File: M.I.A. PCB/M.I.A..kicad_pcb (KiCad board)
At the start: 6 copper layers, 50.8 x 106.6 mm, 159 parts, among them J1 USB_C_Receptacle_USB2.0_16P, J10 Conn_01x03, J11 Conn_01x03, J12 Conn_Coaxial, J12 Screw_Terminal_01x02, J13 Screw_Terminal_01x02, J14 Screw_Terminal_01x02, J15 Screw_Terminal_01x02, J16 Screw_Terminal_01x02, J17 Screw_Terminal_01x02, J18 Screw_Terminal_01x02, J19 Conn_01x08_Socket, J2 Conn_01x02_Pin, J20 Screw_Terminal_01x02, J21 Conn_01x04_Socket, J22 Conn_01x04_Socket, J3 Conn_01x03, J4 Conn_01x03, J5 Conn_01x03, J6 Conn_01x03, J7 MSD-4-A, J8 Conn_01x03, J9 Conn_01x03, Q1 AO3400A, Q2 AO3400A, Q3 AO3400A, Q4 AO3400A, SW1 SW_Push, SW2 SW_Push, U1 W25Q128JVS, U10 AP2112K-3.3, U11 INA219AxDCN, U12 AP62150WU, U13 TPS2121RUXR, U14 AP62150WU, U15 74AHC541, U2 RP2350B-QFN80, U3 MMC5983MA, U4 ICM-45686, U5 MS5611-01BA, U6 TMP117xxDRV, U7 MAX-M10S, U8 KX134-1211, U9 TPS2121RUXR, Y1 ABM8-272-T3

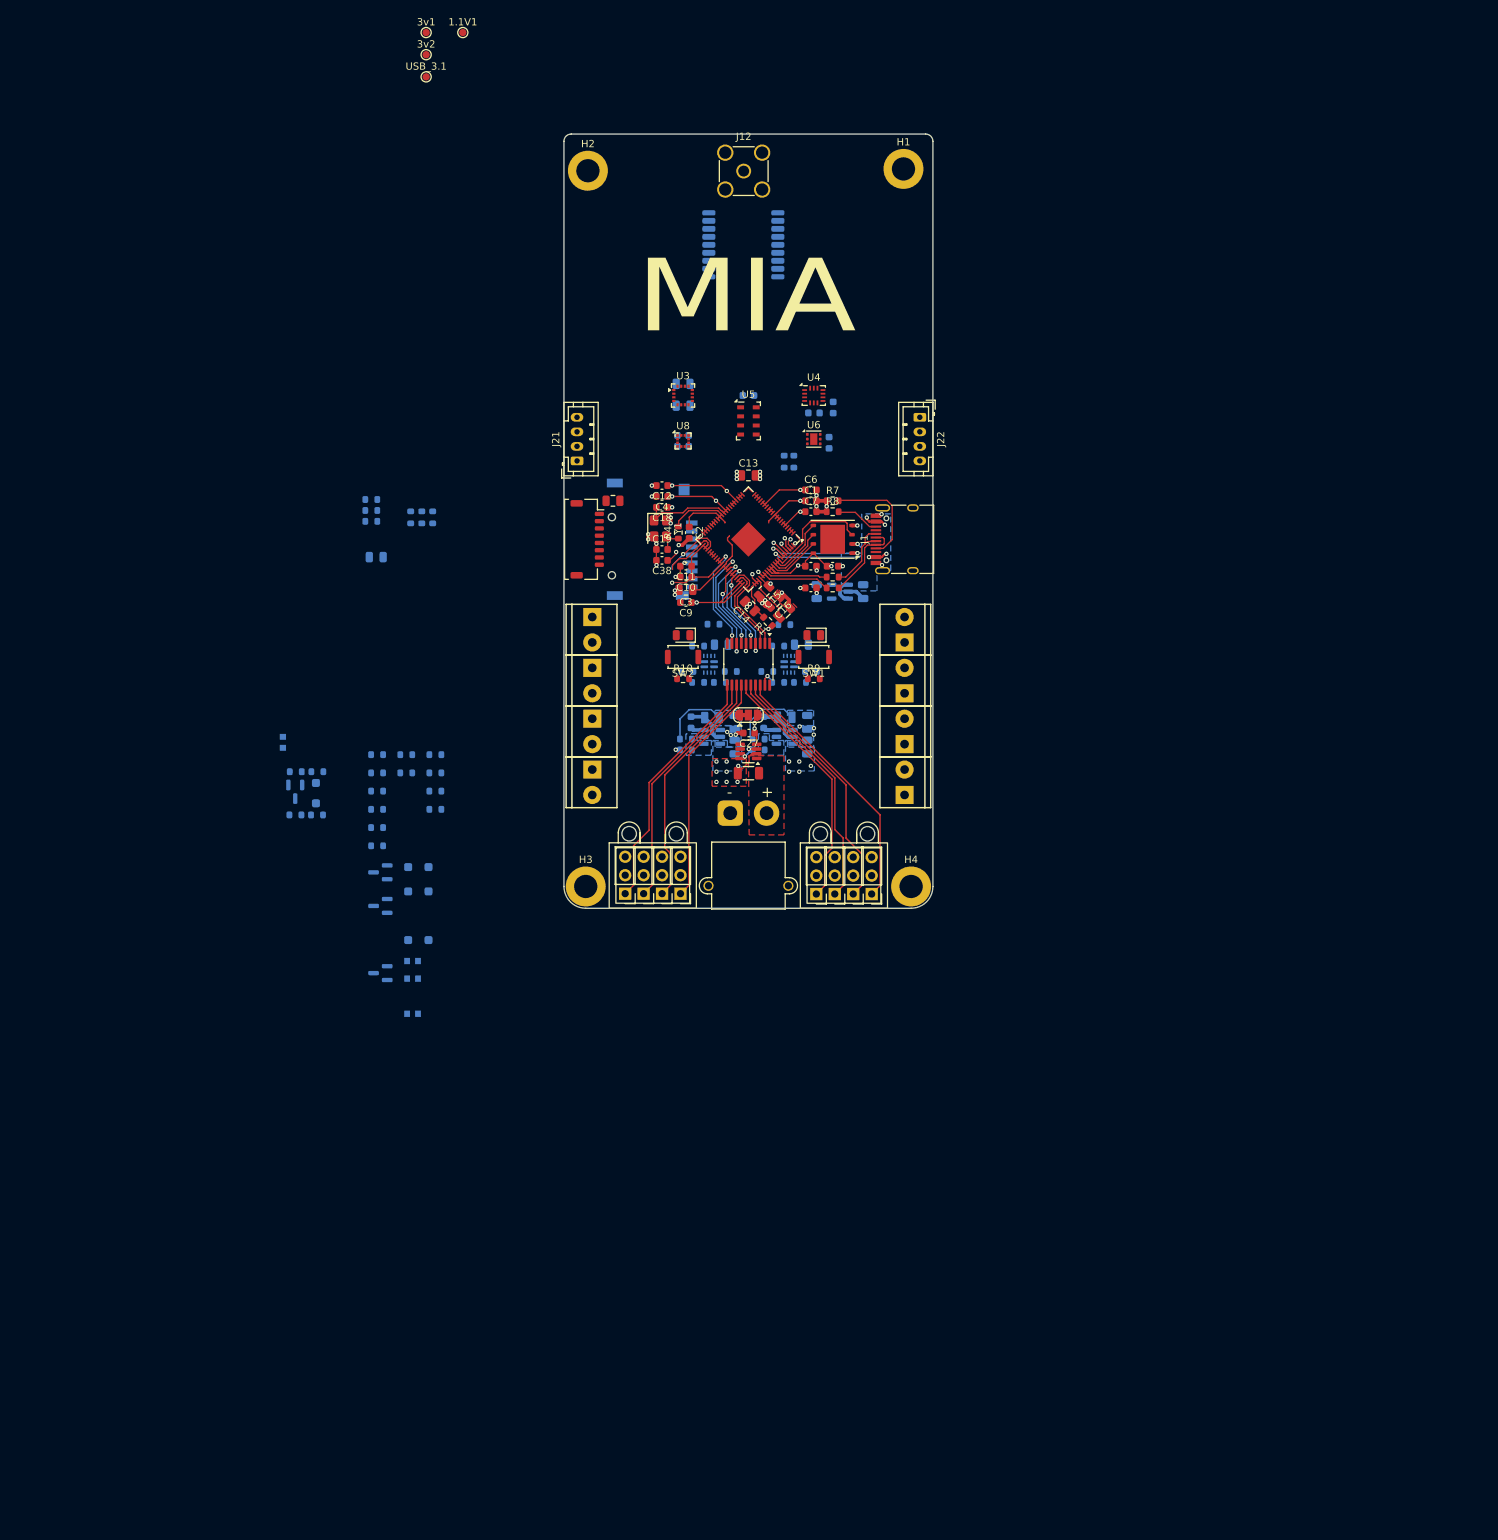
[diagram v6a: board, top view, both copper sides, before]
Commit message: Wired Sensors
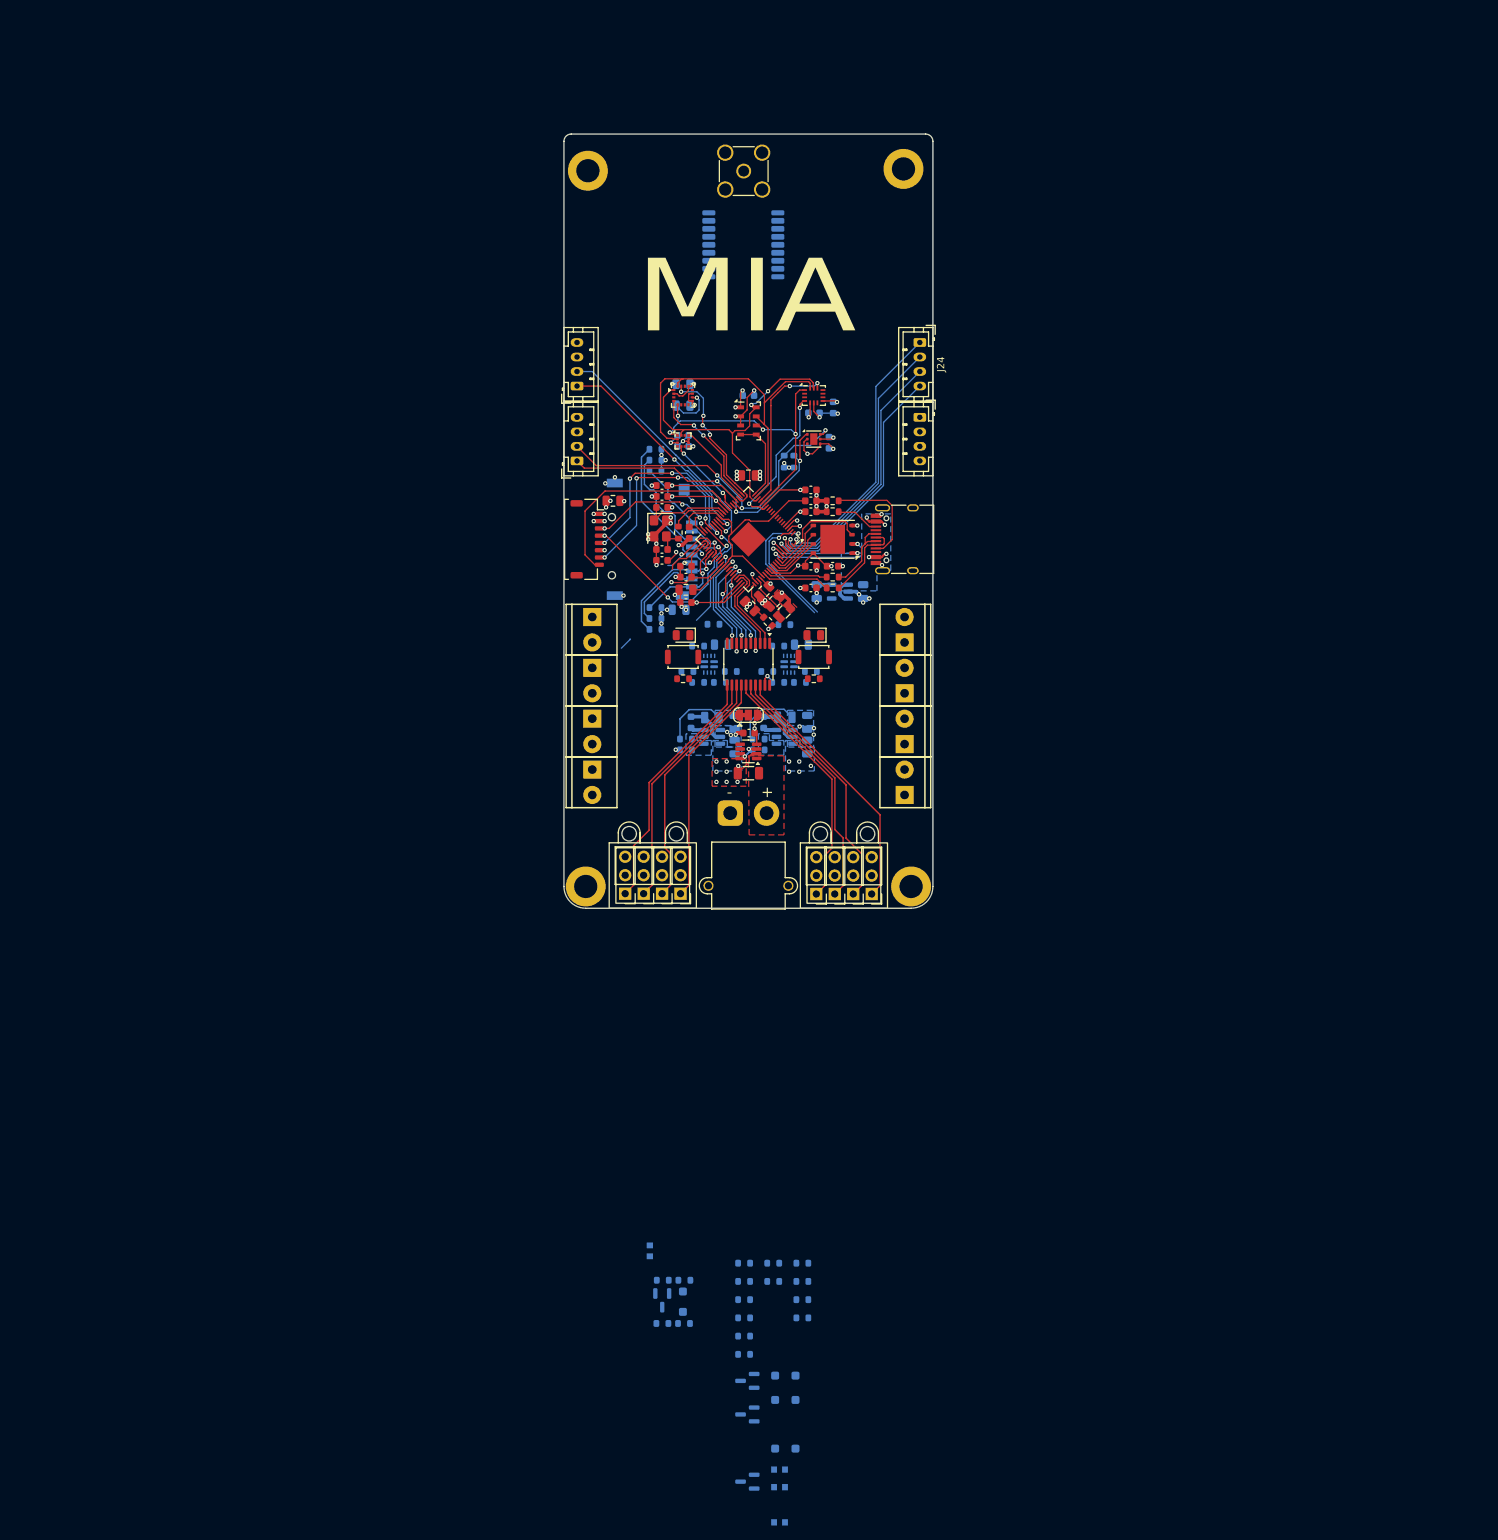
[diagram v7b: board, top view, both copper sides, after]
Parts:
- removed 1.1V1, 3v1, 3v2, USB_3.1: TestPoint, TestPoint:TestPoint_Pad_D1.0mm
- added J23: Conn_01x04_Socket, Connector_JST:JST_PH_B4B-PH-K_1x04_P2.00mm_Vertical, F.Cu at (21.8, 49.7)
- added J24: Conn_01x04_Socket, Connector_JST:JST_PH_B4B-PH-K_1x04_P2.00mm_Vertical, F.Cu at (69.0, 43.7)
- moved D4 86.3 mm to (50.5, 189.3)
- moved D5 86.3 mm to (36.4, 175.8)
- moved F3 86.3 mm to (31.8, 168.8)
- moved Q1 86.3 mm to (45.3, 186.7)
- moved Q2 86.3 mm to (45.3, 191.3)
- moved Q3 86.3 mm to (33.5, 175.6)
- moved Q4 86.3 mm to (45.3, 200.6)
- moved R34 86.3 mm to (44.8, 170.5)
- moved R35 86.3 mm to (44.8, 173.0)
- moved R36 86.3 mm to (44.8, 175.5)
- moved R37 86.3 mm to (44.8, 178.0)
- moved R38 86.3 mm to (44.8, 180.5)
- moved R39 86.3 mm to (44.8, 183.0)
- moved R40 86.3 mm to (48.8, 170.5)
- moved R41 86.3 mm to (48.8, 173.0)
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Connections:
- U2 pad 1: unconnected-(U2-GPIO4-Pad1) -> IGN_4
- U2 pad 14: unconnected-(U2-GPIO15-Pad14) -> IMU_INT1
- U2 pad 16: unconnected-(U2-GPIO16-Pad16) -> SPI_MISO_SEN
- U2 pad 17: unconnected-(U2-GPIO17-Pad17) -> IMU_CS
- U2 pad 18: unconnected-(U2-GPIO18-Pad18) -> SPI_SCK_SEN
- U2 pad 19: unconnected-(U2-GPIO19-Pad19) -> SPI_MOSI_SEN
- U2 pad 2: unconnected-(U2-GPIO5-Pad2) -> IGN_3
- U2 pad 20: unconnected-(U2-GPIO20-Pad20) -> BAR_CS
- U2 pad 21: unconnected-(U2-GPIO21-Pad21) -> MAG_CS
- U2 pad 22: unconnected-(U2-GPIO22-Pad22) -> ACC_CS
- U2 pad 23: unconnected-(U2-GPIO23-Pad23) -> MAG_INT
- U2 pad 25: unconnected-(U2-GPIO24-Pad25) -> SDA
- U2 pad 26: unconnected-(U2-GPIO25-Pad26) -> SCL
- U2 pad 27: unconnected-(U2-GPIO26-Pad27) -> ACC_INT
- U2 pad 28: unconnected-(U2-GPIO27-Pad28) -> RST_TLM
- U2 pad 33: unconnected-(U2-SWCLK-Pad33) -> SWCLK
- U2 pad 34: unconnected-(U2-SWDIO-Pad34) -> SWDIO
- U2 pad 36: unconnected-(U2-GPIO28-Pad36) -> SPI_MISO_TLM
- U2 pad 37: unconnected-(U2-GPIO29-Pad37) -> SPI_CS_TLM
- U2 pad 38: unconnected-(U2-GPIO30-Pad38) -> SPI_SCK_TLM
- U2 pad 39: IGN_4 -> SPI_MOSI_TLM
- U2 pad 40: IGN_3 -> D0_TLM
- U2 pad 77: unconnected-(U2-GPIO0-Pad77) -> GPIO1
- U2 pad 78: unconnected-(U2-GPIO1-Pad78) -> GPIO2
- U2 pad 79: unconnected-(U2-GPIO2-Pad79) -> GPIO3
- U2 pad 80: unconnected-(U2-GPIO3-Pad80) -> GPIO4
- U4 pad 9: IMU_INT2 -> unconnected-(U4-INT2/FSYNC/CLKIN-Pad9)
- U8 pad 4: ACC_TRIG -> GND
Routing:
- net SPI_MOSI_SEN: track 0.00 -> 51.1 mm
- net SDA: track 0.00 -> 47.2 mm, vias 0 -> 3
- net SPI_SCK_SEN: track 0.00 -> 45.1 mm, vias 0 -> 2
- net SCL: track 0.00 -> 44.6 mm, vias 0 -> 3
- net SPI_MISO_SEN: track 0.00 -> 42.3 mm, vias 0 -> 4
- net GND: track 55.0 -> 94.9 mm, vias 41 -> 62
- net GPIO4: track 0.00 -> 37.6 mm, vias 0 -> 1
- net GPIO2: track 0.00 -> 37.6 mm, vias 0 -> 1
- net GPIO3: track 0.00 -> 37.5 mm, vias 0 -> 1
- net GPIO1: track 0.00 -> 35.3 mm, vias 0 -> 1
- net SWDIO: track 0.00 -> 34.5 mm, vias 0 -> 1
- net +3.3V: track 81.2 -> 112.7 mm, vias 20 -> 39
- net SWCLK: track 0.00 -> 31.2 mm, vias 0 -> 2
- net RST_TLM: track 0.00 -> 30.6 mm
- net SPI_MISO_TLM: track 0.00 -> 30.6 mm, vias 0 -> 4
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- removed copper zone on In2.Cu, net +1V1

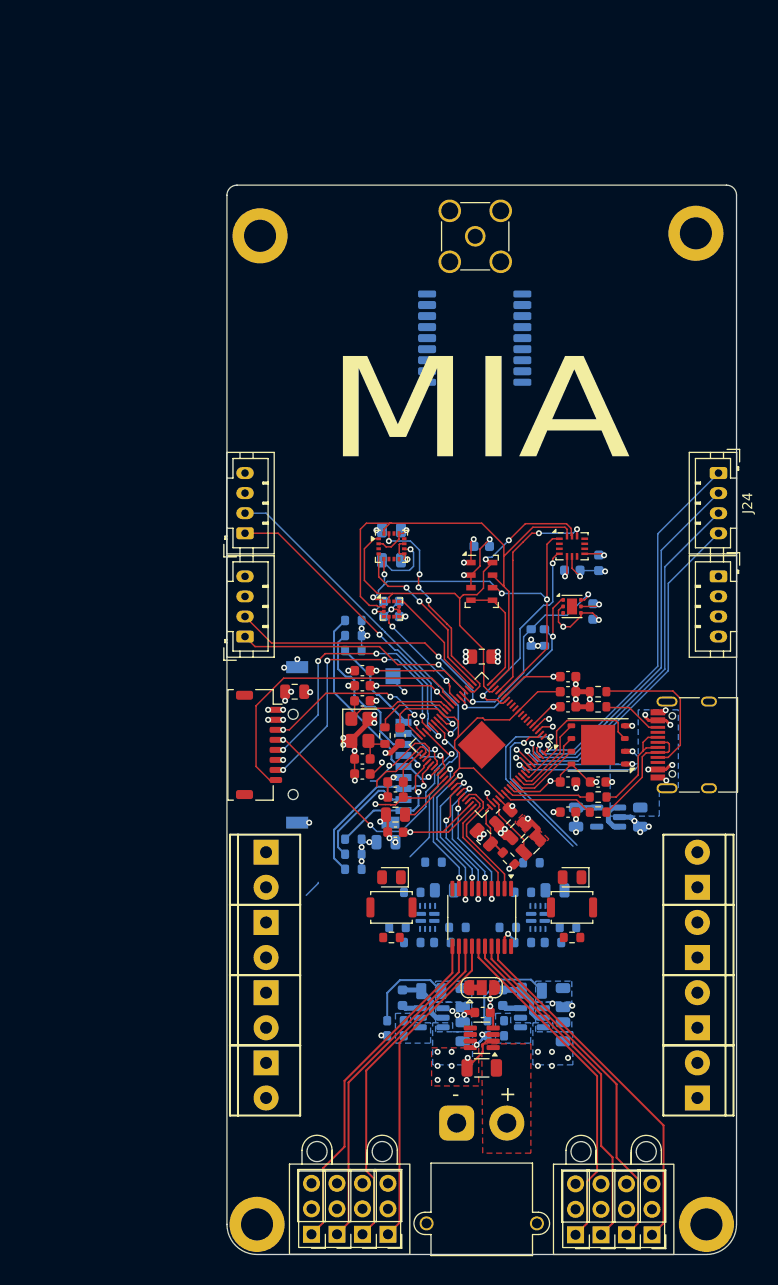
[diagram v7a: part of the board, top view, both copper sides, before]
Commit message: routed continuity sensing and pwm routing fixed
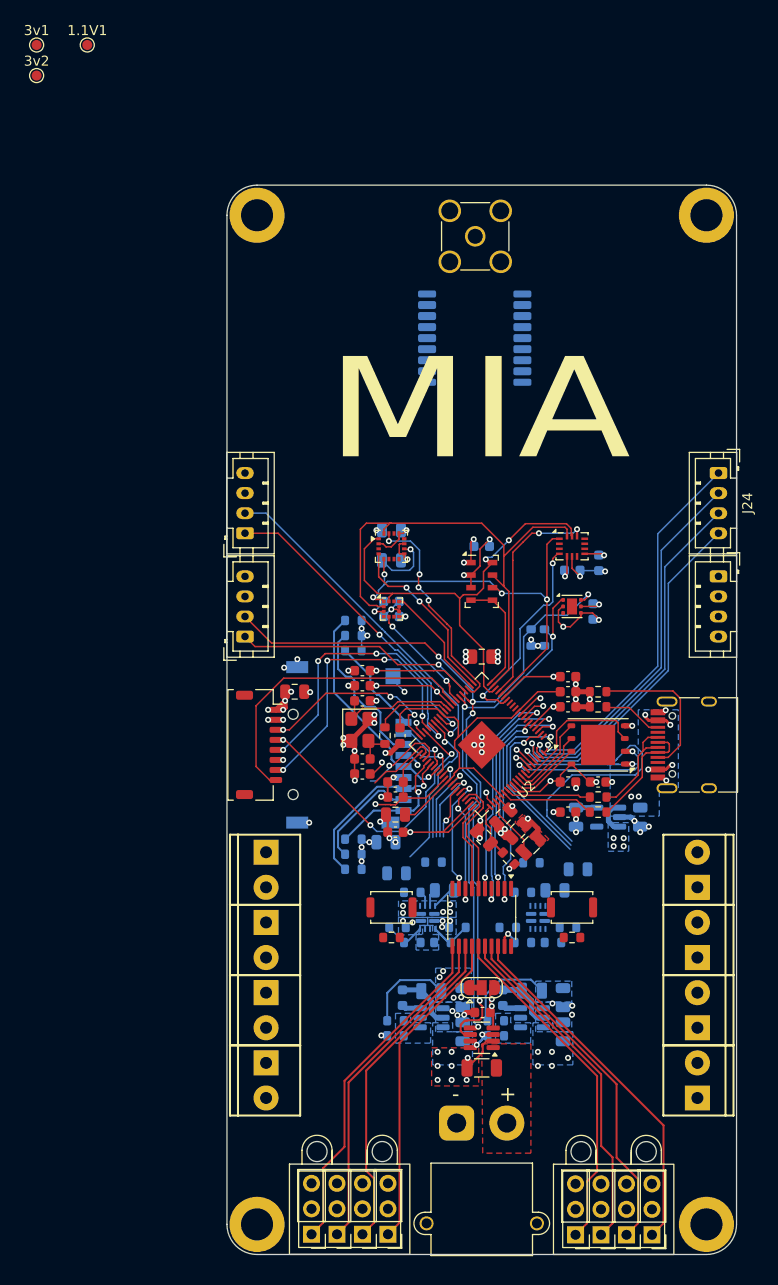
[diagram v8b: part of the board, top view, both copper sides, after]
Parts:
- added 1.1V1: TestPoint, TestPoint:TestPoint_Pad_D1.0mm, F.Cu at (6.08, 1.02)
- added 3v1: TestPoint, TestPoint:TestPoint_Pad_D1.0mm, F.Cu at (1.02, 1.02)
- added 3v2: TestPoint, TestPoint:TestPoint_Pad_D1.0mm, F.Cu at (1.02, 4.08)
- D1, D2: moved to B.Cu
- moved H1 2.08 mm to (67.8, 18.0)
- moved H2 2.07 mm to (23.0, 18.0)
- moved D1 1.00 mm to (55.0, 83.2), turned to 0 degrees
- moved D2 0.64 mm to (36.9, 83.6), turned to 0 degrees
- turned C34 to 0 degrees
- turned R25 to 180 degrees
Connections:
- U2 pad 3: unconnected-(U2-GPIO6-Pad3) -> PWM2
- U2 pad 4: unconnected-(U2-GPIO7-Pad4) -> PWM3
- U2 pad 49: PWM8 -> Cont_Sense4
- U2 pad 52: PWM7 -> Cont_Sense3
- U2 pad 53: PWM6 -> Cont_Sense2
- U2 pad 54: PWM5 -> Cont_Sense1
- U2 pad 55: PWM4 -> PWM8
- U2 pad 56: PWM3 -> PWM7
- U2 pad 57: PWM1 -> PWM5
- U2 pad 58: PWM2 -> PWM6
- U2 pad 6: unconnected-(U2-GPIO8-Pad6) -> PWM1
- U2 pad 7: unconnected-(U2-GPIO9-Pad7) -> PWM4
- U2 pad 81: unconnected-(U2-GND-Pad81) -> GND
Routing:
- net SDA: track 47.2 -> 84.8 mm, vias 3 -> 5
- net SCL: track 44.6 -> 78.7 mm, vias 3 -> 4
- net /QSPI_SS: track 14.4 -> 36.5 mm
- net PWM3: track 12.9 -> 25.1 mm
- net PWM2: track 12.2 -> 22.5 mm, vias 0 -> 2
- net PWM4: track 13.0 -> 22.0 mm
- net Cont_Sense4: track 0.00 -> 8.68 mm, vias 0 -> 1
- net Cont_Sense3: track 0.00 -> 8.31 mm, vias 0 -> 1
- net PWM1: track 13.2 -> 21.3 mm, vias 0 -> 2
- net Cont_Sense2: track 0.00 -> 7.74 mm, vias 0 -> 1
- net Net-(U13-CP2): track 0.00 -> 6.14 mm
- net Cont_Sense1: track 0.00 -> 5.23 mm, vias 0 -> 1
- net PWM7: track 16.9 -> 11.9 mm
- net GND: track 94.9 -> 99.3 mm, vias 62 -> 66
- net Net-(U13-PR1): track 0.00 -> 4.27 mm
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- added copper zone on B.Cu, net +5V
- added copper zone on B.Cu, net 3.3v_Batt
- added copper zone on In3.Cu, net 5v_Batt
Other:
- outline, holes or cut-outs redrawn
- board text added: "move ldo and maybe buttons"
